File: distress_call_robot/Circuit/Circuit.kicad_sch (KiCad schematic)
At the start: 7 parts, among them M1 JST-2p, M2 JST-2p, U1 L293D

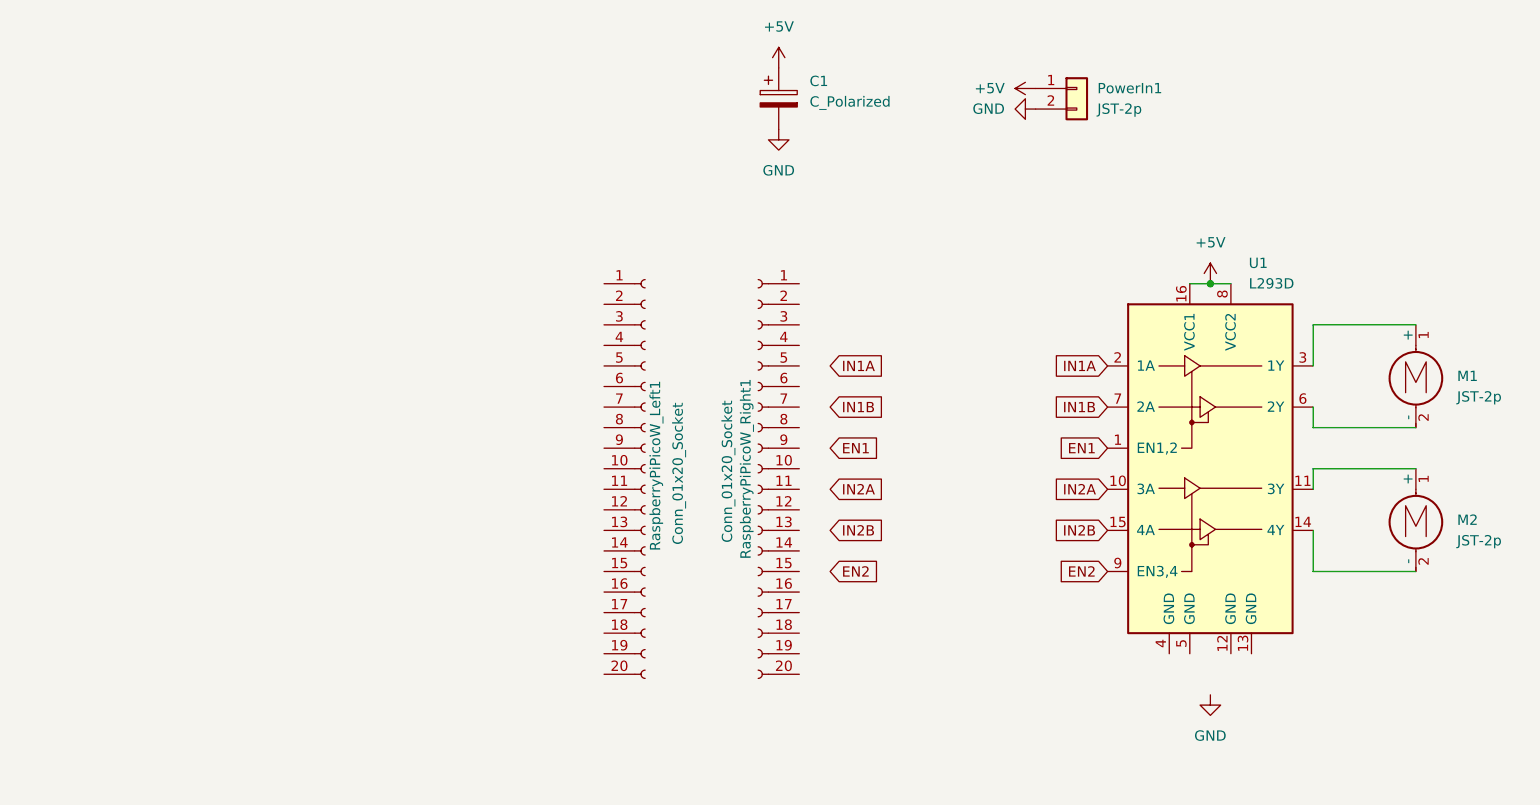
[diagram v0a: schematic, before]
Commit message: finished distress robot PCB and DC motor differential control code
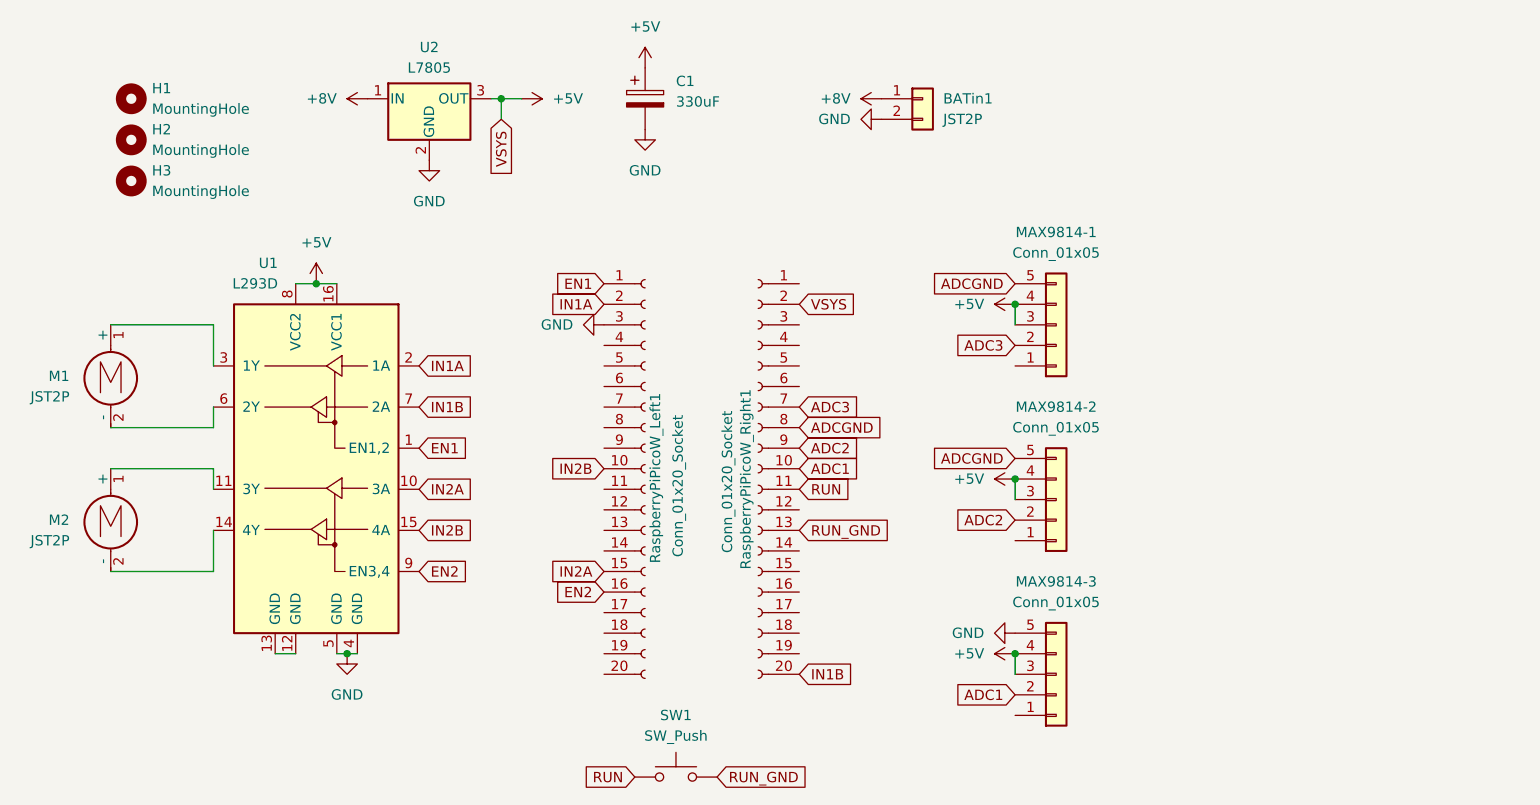
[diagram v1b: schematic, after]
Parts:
- added H1, H2, H3: MountingHole, MountingHole:MountingHole_3.2mm_M3_DIN965_Pad, symbol Mechanical:MountingHole
- added MAX9814-1, MAX9814-2, MAX9814-3: Conn_01x05, Connector_PinSocket_2.54mm:PinSocket_1x05_P2.54mm_Vertical, symbol Connector_Generic:Conn_01x05
- added SW1: SW_Push, Resistor_THT:R_Axial_DIN0204_L3.6mm_D1.6mm_P5.08mm_Vertical, symbol Switch:SW_Push
- added U2: L7805, Package_TO_SOT_THT:TO-220-3_Vertical, symbol Regulator_Linear:L7805
- BATin1: renamed from PowerIn1; value JST-2p -> JST2P
- C1: value C_Polarized -> 330uF; footprint (none) -> Capacitor_THT:CP_Radial_D6.3mm_P2.50mm
- M1, M2: value JST-2p -> JST2P
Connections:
- net +5V: now also RaspberryPiPicoW_Right1.2 (Pin_2), MAX9814-1.3 (Pin_3), MAX9814-1.4 (Pin_4), MAX9814-2.3 (Pin_3), MAX9814-2.4 (Pin_4), MAX9814-3.3 (Pin_3), MAX9814-3.4 (Pin_4), U2.3 (OUT); no longer BATin1.1 (Pin_1)
- net EN1: now also RaspberryPiPicoW_Left1.1 (Pin_1)
- net EN2: now also RaspberryPiPicoW_Left1.16 (Pin_16)
- net GND: now also RaspberryPiPicoW_Left1.3 (Pin_3), U1.4 (GND), U1.5 (GND), MAX9814-3.5 (Pin_5), U2.2 (GND)
- net IN1A: now also RaspberryPiPicoW_Left1.2 (Pin_2)
- net IN1B: now also RaspberryPiPicoW_Right1.20 (Pin_20)
- net IN2A: now also RaspberryPiPicoW_Left1.15 (Pin_15)
- net IN2B: now also RaspberryPiPicoW_Left1.10 (Pin_10)
- net ADC1: now reaches RaspberryPiPicoW_Right1.10 (Pin_10)
- net ADC1: now also MAX9814-3.2 (Pin_2)
- net RUN: now reaches RaspberryPiPicoW_Right1.11 (Pin_11)
- net RUN: now also SW1.1
- net RUN_GND: now reaches RaspberryPiPicoW_Right1.13 (Pin_13)
- net RUN_GND: now also SW1.2
- net ADC3: now reaches RaspberryPiPicoW_Right1.7 (Pin_7)
- net ADC3: now also MAX9814-1.2 (Pin_2)
- net ADCGND: now reaches RaspberryPiPicoW_Right1.8 (Pin_8)
- net ADCGND: now also MAX9814-1.5 (Pin_5), MAX9814-2.5 (Pin_5)
- net ADC2: now reaches RaspberryPiPicoW_Right1.9 (Pin_9)
- net ADC2: now also MAX9814-2.2 (Pin_2)
- net at U1.12 (GND): now also U1.13 (GND)
- new net +8V: BATin1.1 (Pin_1), U2.1 (IN)
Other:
- moved on the sheet: BATin1, C1, M1, M2, U1
